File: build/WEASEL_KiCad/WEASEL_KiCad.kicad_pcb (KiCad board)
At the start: 2 copper layers, 335.1 x 620 mm, 314 parts, among them J1 MIDI IN, J10 PLSR_OUTPUT2, J11 PLSR_OUTPUT3, J12 RNDM_OUTPUT1, J13 RNDM_OUTPUT2, J14 RNDM_OUTPUT3, J15 PLSR_PERIODCTRL, J16 MODOSC_FREQCTRL, J17 MODOSC_MODCTRL, J18 COMPOSC_PITCHCTRL, J19 COMPOSC_WAVEFOLDERCTRL, J2 STEREO_OUTPUT, J20 LPG_LEVEL1CTRL, J21 LPG_LEVEL2CTRL, J22 Jack-DC, J3 SEQ_OUTPUT1, J4 SEQ_OUTPUT2, J5 SEQ_OUTPUT3, J6 EG_OUTPUT1, J7 EG_OUTPUT2, J8 EG_OUTPUT3, J9 PLSR_OUTPUT1, SW1 SEQ_TRIGGERSELECT, SW10 COMPLEXOSC_POLARITY, SW11 COMPLEXOSC_WAVETOGGLE, SW12 LPG_GATE1MODE, SW13 LPG_GATE2MODE, SW14 RNDMVOLTAGE_TRIGGERSELECT, SW15 CLOCK_SYNCTOGGLE, SW16 SQ_TOGGLESTEP1, SW17 SQ_TOGGLESTEP2, SW18 SQ_TOGGLESTEP3, SW19 SQ_TOGGLESTEP4, SW2 SEQ_STAGES, SW20 SQ_TOGGLESTEP5, SW3 EG_TRIGGERSELECT, SW4 EG_MODESELECT, SW5 PLSR_TRIGGERSELECT, SW6 PLSR_MODE, SW7 MODOSC_MODULATIONMODE, SW8 MODOSC_WAVEFORMTOGGLE, SW9 OSCILLATOR_MIDITOGGLE, U1 AW9523B, U10 AW9523B, U11 AW9523B, U2 AW9523B, U3 6N138, U4 CD74HC4067M, U5 CD74HC4067M, U6 74HC165, U7 74HC165, U8 74HC165, U9 74HC165

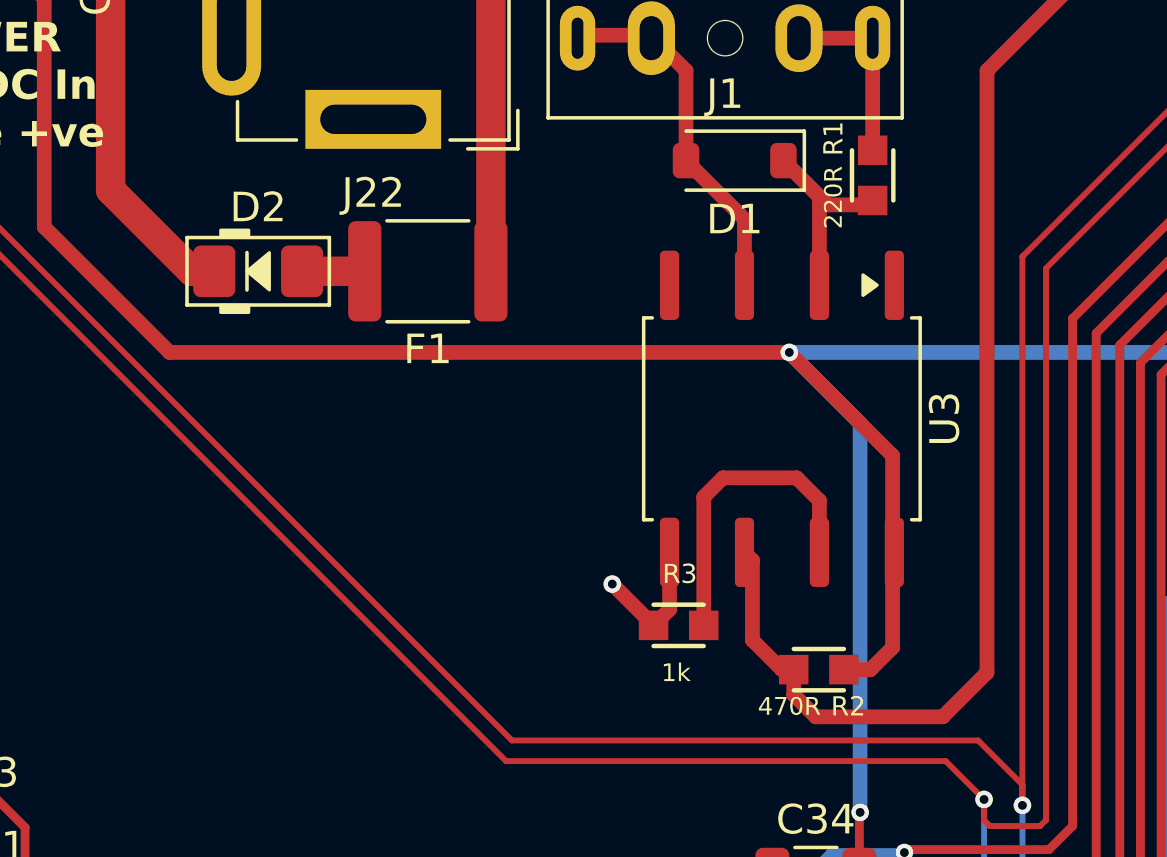
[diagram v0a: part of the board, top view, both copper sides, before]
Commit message: PCB Footprint Updates
- changed 6N138 to DIP-8 package
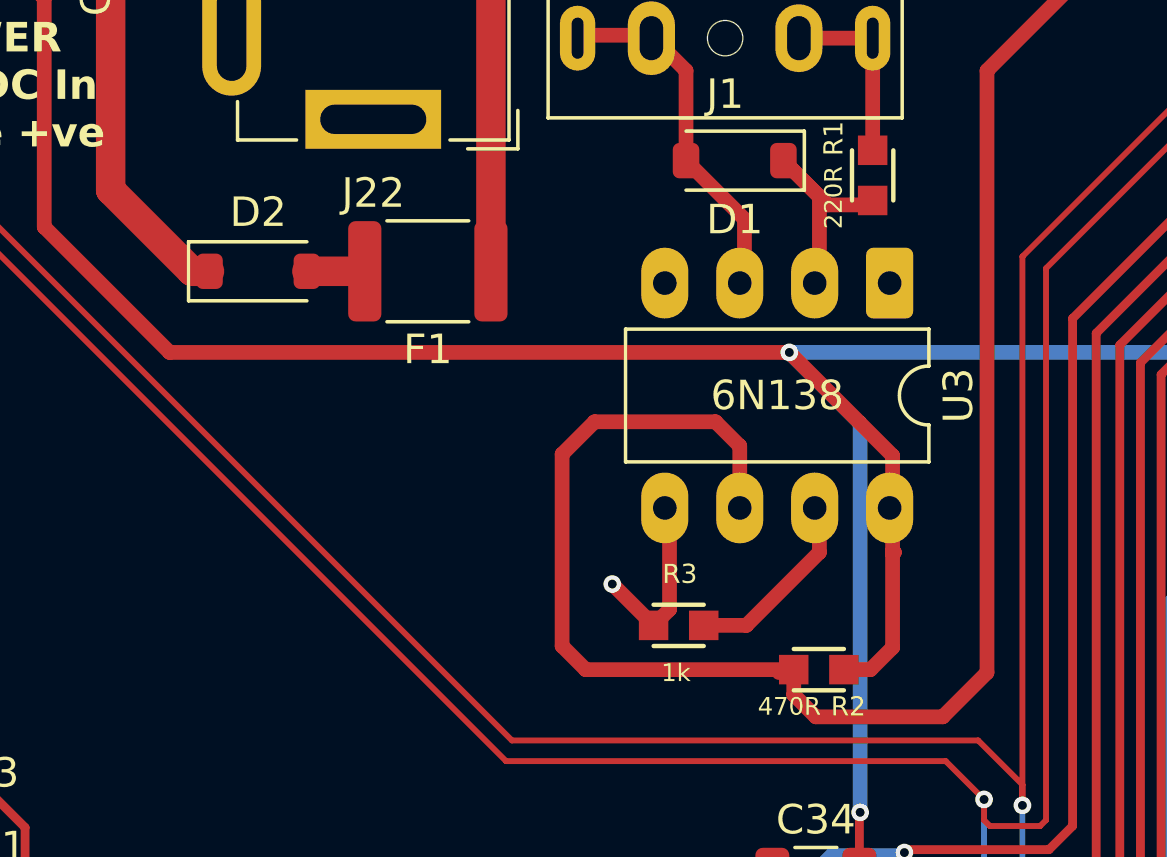
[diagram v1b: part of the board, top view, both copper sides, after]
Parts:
- D2: footprint PCM_Diode_SMD_AKL:D_1206_3216Metric_Pad1.42x1.75mm_HandSolder -> Diode_SMD:D_SOD-123
- U3: footprint Package_SO:SOP-8_6.62x9.15mm_P2.54mm -> Package_DIP:DIP-8_W7.62mm_LongPads
- moved U3 5.87 mm to (115.4, 31.9)
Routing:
- net MIDI_INPUT: track 186.0 -> 204.8 mm
- net Net-(U3-VO1): track 10.6 -> 6.70 mm
- net DGND: track 346.2 -> 347.8 mm
